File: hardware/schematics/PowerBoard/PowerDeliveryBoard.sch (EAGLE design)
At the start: 17 parts

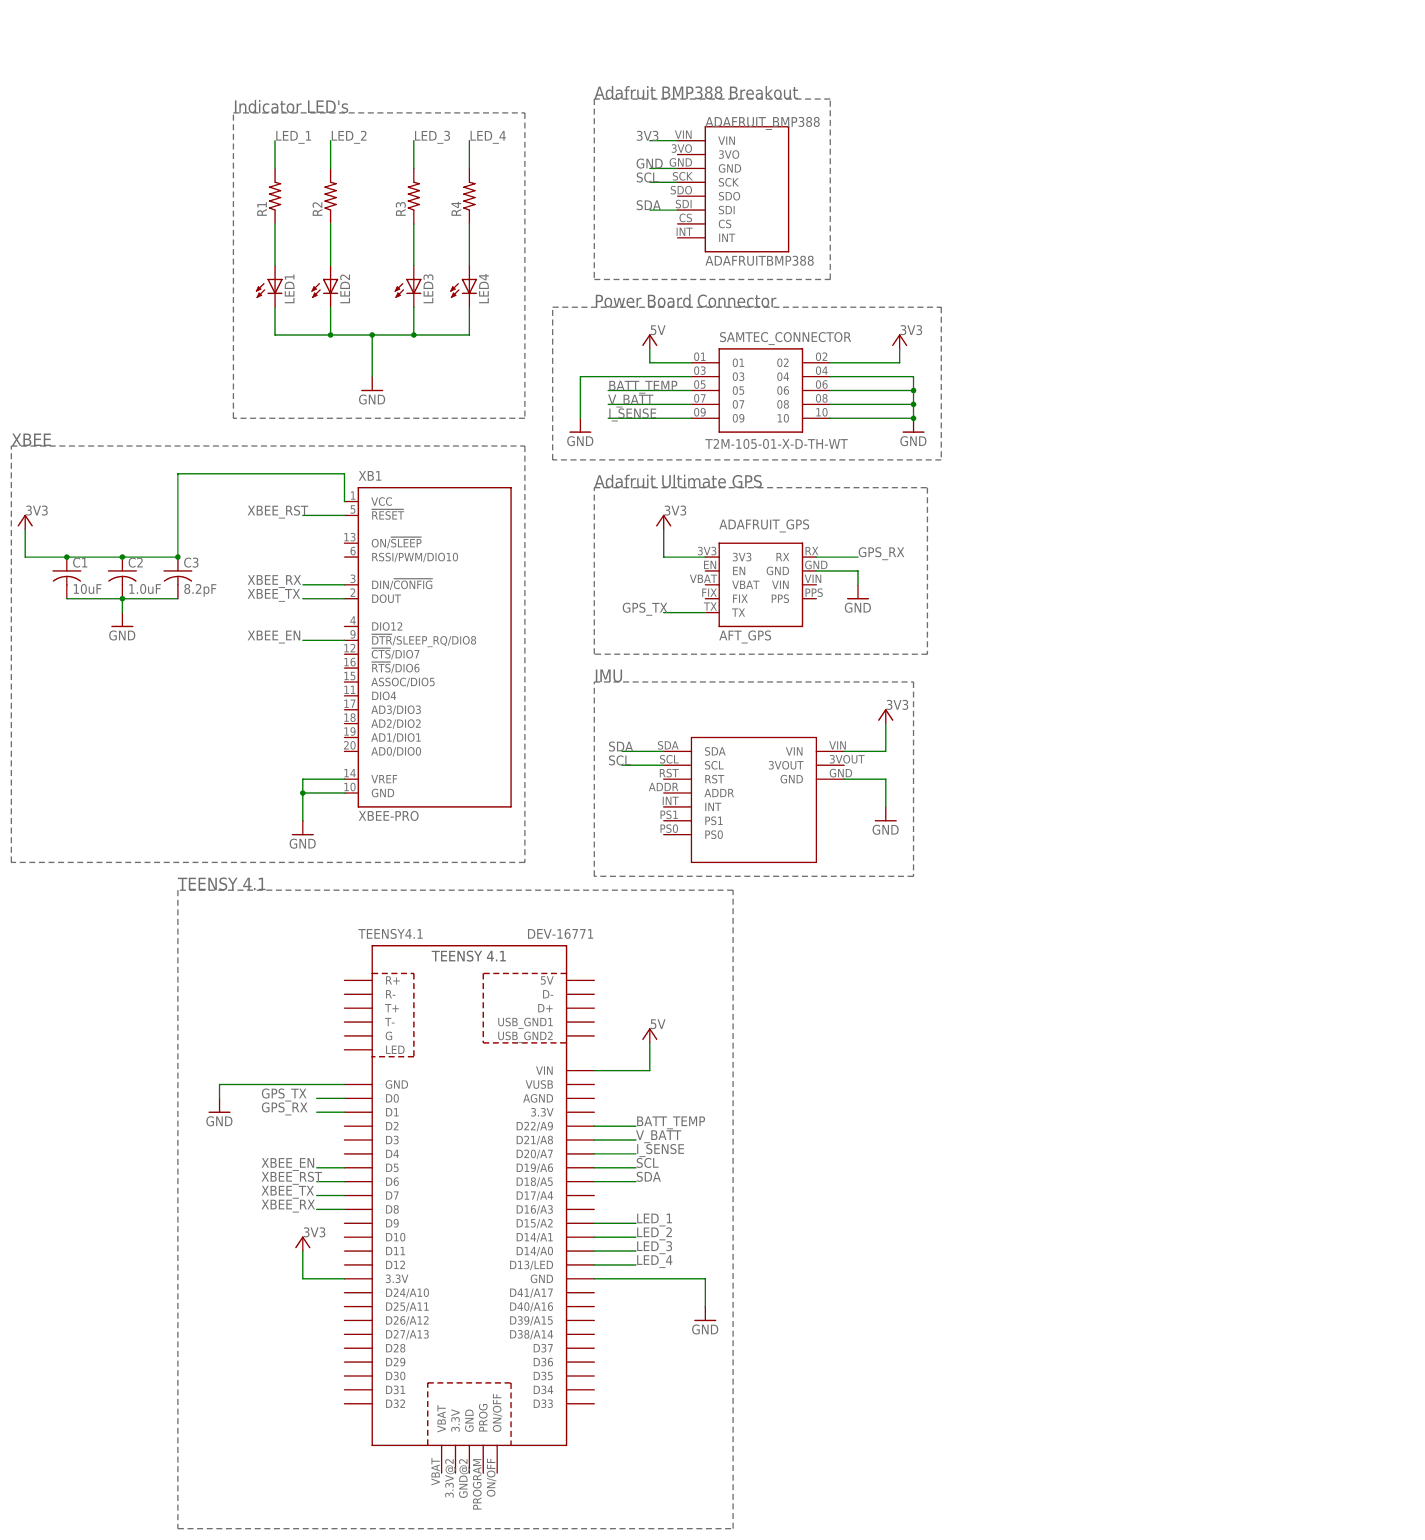
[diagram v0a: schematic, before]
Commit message: Add Power Board | Change MB Connector Pins | Move Old PDB.sch to PCBs Folder
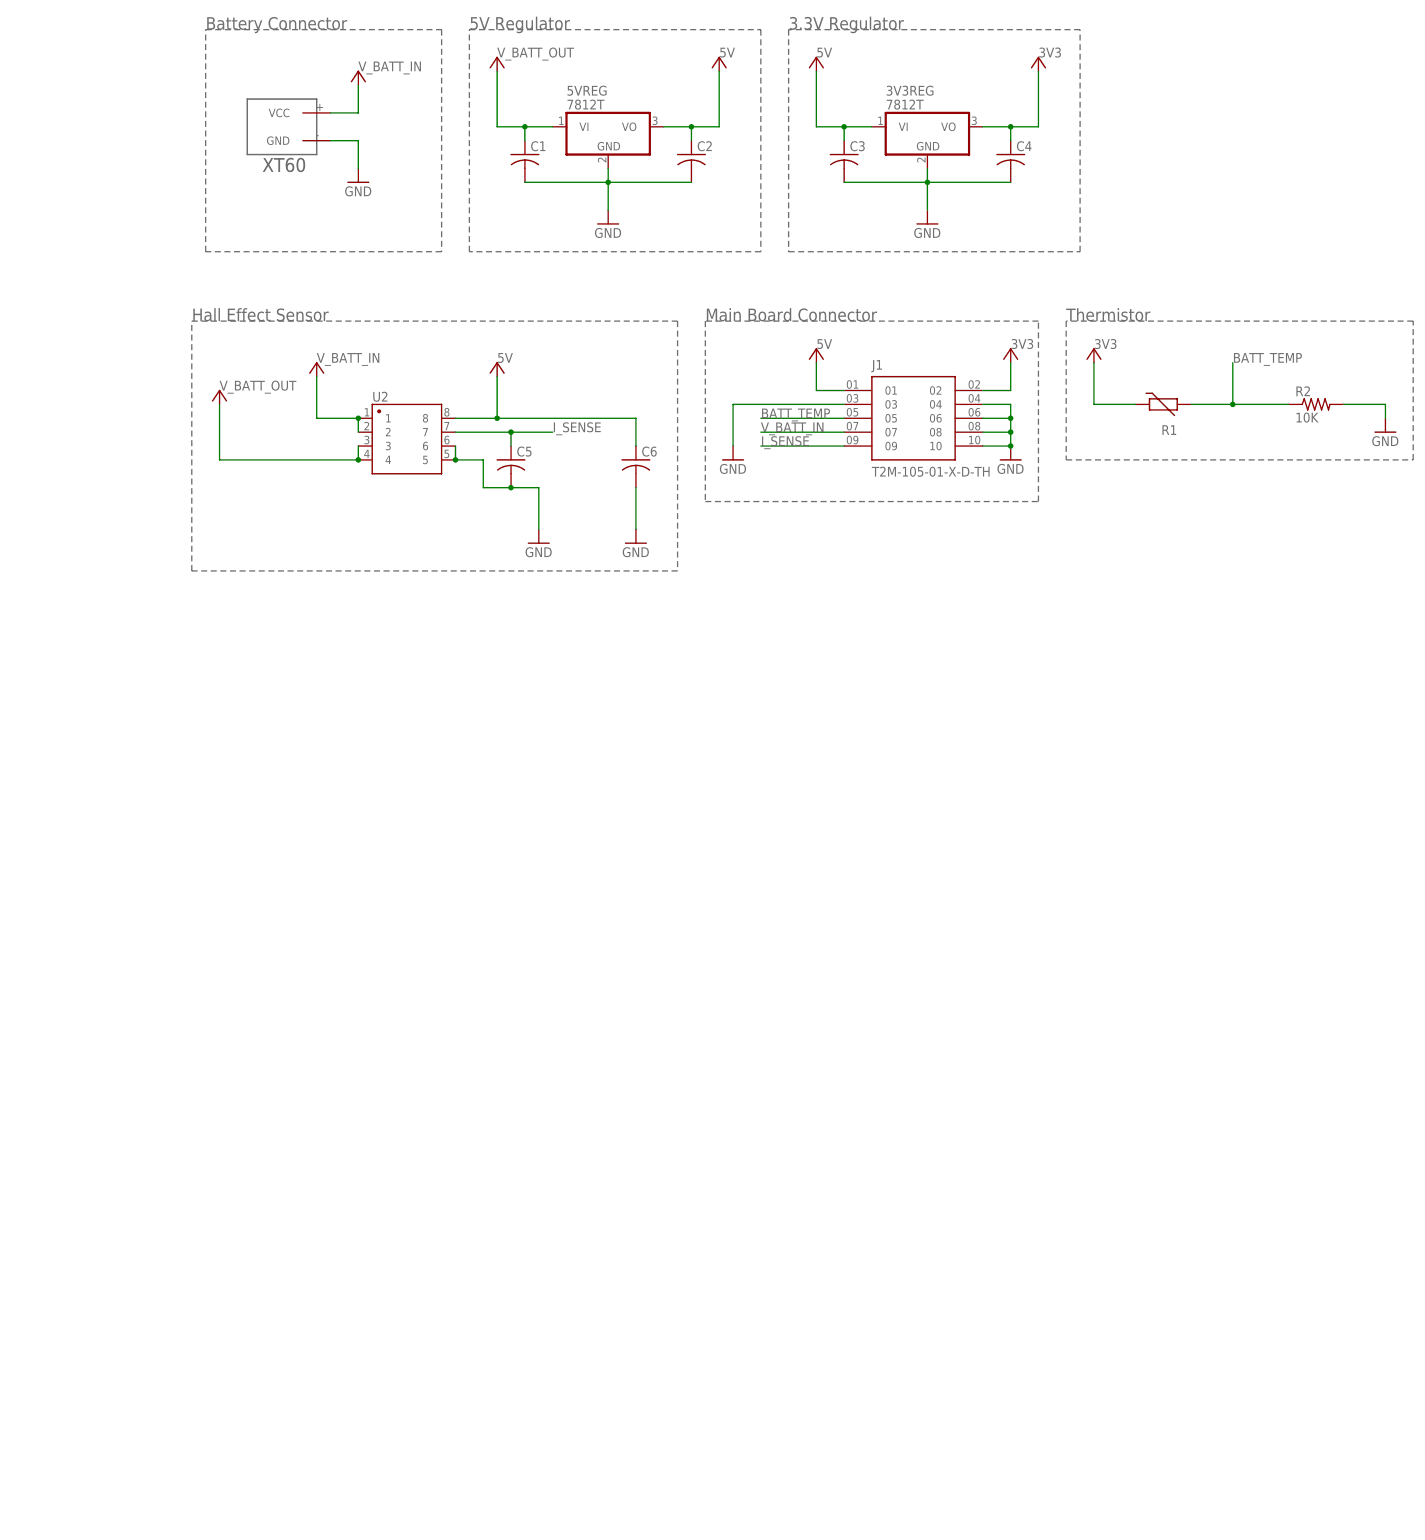
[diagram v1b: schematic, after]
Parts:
- removed ADAFRUIT_BMP388: ADAFRUITBMP388, adafruit BMP388:ADAFRUITBMP388
- removed ADAFRUIT_GPS: AFT_GPS, adafruit_Ultimate_GPS_Breakout:AFT_GPS
- removed LED1, LED2, LED3, LED4: (no value), adafruit(seeIMUBreakout):LED5MM
- removed R3, R4: (no value), adafruit(seeIMUBreakout):R-US_R0805
- removed SAMTEC_CONNECTOR: T2M-105-01-X-D-TH-WT, T2M-105-01-X-D-TH-WT:T2M-105-01-X-D-TH-WT
- removed TEENSY4.1: DEV-16771, DEV-16771(Teensy 4.1):DEV-16771
- removed U$1: IMU_BREAKOUT, adafruit(seeIMUBreakout):IMU_BREAKOUT
- removed XB1: XBEE-PRO, xbee:XBEE-PRO
- added 3V3REG, 5VREG: 7812T, adafruit(seeIMUBreakout):7812T
- added C4, C5, C6: (no value), adafruit(seeIMUBreakout):C-USC0805
- added J1: T2M-105-01-X-D-TH, T2M-105-01-X-D-TH:T2M-105-01-X-D-TH
- added U$3: XT60_XT60, XT60_LipoConnector:XT60_XT60
- added U2: ASC723, SparkFun-Retired:GENERIC-SOIC8MSGEQ7N-FILTER
- C1: value 10uF -> (none)
- C2: value 1.0uF -> (none)
- C3: value 8.2pF -> (none)
- R1: value (none) -> THERMISTOR-5; device adafruit(seeIMUBreakout):R-US_R0805 -> varistor:THERMISTOR-5
- R2: value (none) -> 10K
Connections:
- removed net GPS_RX: ADAFRUIT_GPS.RX, TEENSY4.1.D1
- removed net GPS_TX: ADAFRUIT_GPS.TX, TEENSY4.1.D0
- removed net LED_1: R1.2, TEENSY4.1.D15/A2
- removed net LED_2: R2.2, TEENSY4.1.D14/A1
- removed net LED_3: R3.2, TEENSY4.1.D14/A0
- removed net LED_4: R4.2, TEENSY4.1.D13/LED
- removed net N$10: LED3.A, R3.1
- removed net N$11: LED4.A, R4.1
- removed net N$8: LED1.A, R1.1
- removed net N$9: LED2.A, R2.1
- removed net SCL: ADAFRUIT_BMP388.SCK, TEENSY4.1.D19/A6, U$1.SCL
- removed net SDA: ADAFRUIT_BMP388.SDI, TEENSY4.1.D18/A5, U$1.SDA
- removed net V_BATT: SAMTEC_CONNECTOR.07, TEENSY4.1.D21/A8
- removed net XBEE_EN: TEENSY4.1.D5, XB1.!DTR!/SLEEP_RQ/DIO8
- removed net XBEE_RST: TEENSY4.1.D6, XB1.!RESET
- removed net XBEE_RX: TEENSY4.1.D8, XB1.DIN/!CONFIG
- removed net XBEE_TX: TEENSY4.1.D7, XB1.DOUT
- new net V_BATT_IN: J1.07, U$3.VCC, U2.1, U2.2
- new net V_BATT_OUT: 5VREG.VI, C1.1, U2.3, U2.4
- net 3V3: now also 3V3REG.VO, C4.1, J1.02, R1.1; no longer ADAFRUIT_BMP388.VIN, ADAFRUIT_GPS.3V3, C1.1, C2.1, C3.1, SAMTEC_CONNECTOR.02, TEENSY4.1.3.3V, U$1.VIN, XB1.VCC
- net 5V: now also 3V3REG.VI, 5VREG.VO, C2.1, C3.1, C6.1, J1.01, U2.8; no longer SAMTEC_CONNECTOR.01, TEENSY4.1.VIN
- net BATT_TEMP: now also J1.05, R1.2, R2.1; no longer SAMTEC_CONNECTOR.05, TEENSY4.1.D22/A9
- net GND: now also 3V3REG.GND, 5VREG.GND, C4.2, C5.2, C6.2, J1.03, J1.04, J1.06, J1.08, J1.10, R2.2, U$3.GND, U2.5, U2.6; no longer ADAFRUIT_BMP388.GND, ADAFRUIT_GPS.GND, LED1.C, LED2.C, LED3.C, LED4.C, SAMTEC_CONNECTOR.03, SAMTEC_CONNECTOR.04, SAMTEC_CONNECTOR.06, SAMTEC_CONNECTOR.08, SAMTEC_CONNECTOR.10, TEENSY4.1.GND, TEENSY4.1.GND@1, U$1.GND, XB1.GND, XB1.VREF
- net I_SENSE: now also C5.1, J1.09, U2.7; no longer SAMTEC_CONNECTOR.09, TEENSY4.1.D20/A7
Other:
- note added: "3.3V Regulator"
- note added: "5V Regulator"
- note added: "Battery Connector"
- note added: "Hall Effect Sensor"
- note added: "Main Board Connector"
- note added: "Thermistor"
- note removed: "Adafruit BMP388 Breakout"
- note removed: "Adafruit Ultimate GPS"
- note removed: "IMU"
- note removed: "Indicator LED's"
- note removed: "Power Board Connector"
- note removed: "TEENSY 4.1"
- note removed: "XBEE"
- moved on the sheet: C1, C2, C3, R2
